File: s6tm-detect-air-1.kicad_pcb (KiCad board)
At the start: 2 copper layers, 0 parts

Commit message: pcb: add missing 3dmodels
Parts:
- added C1: 1u, Capacitor_SMD:C_0402_1005Metric, F.Cu at (73.8, 151.6)
- added C10: 0u1, Capacitor_SMD:C_0402_1005Metric, F.Cu at (76.7, 151.6)
- added C11: 0u1, Capacitor_SMD:C_0402_1005Metric, F.Cu at (76.7, 153.6)
- added C12: 0u1, Capacitor_SMD:C_0402_1005Metric, F.Cu at (76.7, 155.6)
- added C13: 0u1, Capacitor_SMD:C_0402_1005Metric, F.Cu at (76.7, 157.5)
- added C14: 0u1, Capacitor_SMD:C_0402_1005Metric, F.Cu at (79.6, 151.6)
- added C15: 1u, Capacitor_SMD:C_0402_1005Metric, F.Cu at (79.6, 153.6)
- added C16: 1u, Capacitor_SMD:C_0402_1005Metric, F.Cu at (79.6, 155.6)
- added C17: 0u1, Capacitor_SMD:C_0402_1005Metric, F.Cu at (79.6, 157.5)
- added C18: 1u, Capacitor_SMD:C_0402_1005Metric, F.Cu at (82.5, 151.6)
- added C19: 0u1, Capacitor_SMD:C_0402_1005Metric, F.Cu at (82.5, 153.6)
- added C2: 10u, Capacitor_SMD:C_0805_2012Metric, F.Cu at (63.3, 163.5)
- added C20: 1u, Capacitor_SMD:C_0402_1005Metric, F.Cu at (82.5, 155.6)
- added C21: 22u, Capacitor_SMD:C_0805_2012Metric, F.Cu at (63.3, 172.5)
- added C22: 0u1, Capacitor_SMD:C_0402_1005Metric, F.Cu at (82.5, 157.5)
- added C23: 22u, Capacitor_SMD:C_0805_2012Metric, F.Cu at (63.3, 175.5)
- added C24: 22u, Capacitor_SMD:C_0805_2012Metric, F.Cu at (63.3, 178.6)
- added C3: 0u1, Capacitor_SMD:C_0402_1005Metric, F.Cu at (73.8, 153.6)
- added C4: 1u, Capacitor_SMD:C_0402_1005Metric, F.Cu at (73.8, 155.6)
- added C5: 10u, Capacitor_SMD:C_0805_2012Metric, F.Cu at (63.3, 166.5)
- added C6: 0u1, Capacitor_SMD:C_0402_1005Metric, F.Cu at (73.8, 157.5)
- added C7: 10u, Capacitor_SMD:C_0805_2012Metric, F.Cu at (63.3, 169.5)
- added C8: 20p, Capacitor_SMD:C_0603_1608Metric, F.Cu at (69.1, 140.4)
- added C9: 20p, Capacitor_SMD:C_0603_1608Metric, F.Cu at (69.1, 142.9)
- added D1: H5VU10U, GLCS:Diode_DFN1006, F.Cu at (59.4, 165.2)
- added D2: H5VU10U, GLCS:Diode_DFN1006, F.Cu at (59.4, 167.2)
- added D3: H5VU10U, GLCS:Diode_DFN1006, F.Cu at (59.4, 169.2)
- added D4: H5VU10U, GLCS:Diode_DFN1006, F.Cu at (59.4, 171.2)
- added D5: H5VU10U, GLCS:Diode_DFN1006, F.Cu at (59.4, 173.2)
- added D6: H5VU10U, GLCS:Diode_DFN1006, F.Cu at (59.4, 175.1)
- added D7: YELLOW, LED_SMD:LED_0805_2012Metric, F.Cu at (55.0, 178.5)
- added D8: SMAJ12A, Diode_SMD:D_SMA, F.Cu at (75.2, 146.5)
- added D9: GREEN, LED_SMD:LED_0805_2012Metric, F.Cu at (55.0, 181.5)
- added FB1: 600Ω@100M, Inductor_SMD:L_0805_2012Metric, F.Cu at (74.7, 159.9)
- added J1: Conn_01x04, Connector_PinHeader_2.54mm:PinHeader_1x04_P2.54mm_Horizontal, F.Cu at (35.5, 152.9)
- added J2: TC2030, Connector:Tag-Connect_TC2030-IDC-NL_2x03_P1.27mm_Vertical, F.Cu at (75.2, 141.7)
- added J3: Conn_01x04, Connector_PinHeader_2.54mm:PinHeader_1x04_P2.54mm_Horizontal, F.Cu at (35.5, 165.2)
- added J4: Conn_01x04, Connector_JST:JST_XH_S4B-XH-A-1_1x04_P2.50mm_Horizontal, F.Cu at (50.1, 155.6)
- added J5: Conn_01x04_Pin, Connector_PinHeader_2.54mm:PinHeader_1x04_P2.54mm_Vertical, F.Cu at (79.2, 164.3)
- added JP1: Jumper_2_Small_Bridged, Jumper:SolderJumper-2_P1.3mm_Open_RoundedPad1.0x1.5mm, F.Cu at (63.2, 181.8)
- added R1: 100, Resistor_SMD:R_0402_1005Metric, F.Cu at (75.4, 163.0)
- added R10: 5k1, Resistor_SMD:R_0402_1005Metric, F.Cu at (75.4, 171.0)
- added R11: 1k, Resistor_SMD:R_0402_1005Metric, F.Cu at (75.4, 172.9)
- added R12: 2k, Resistor_SMD:R_0402_1005Metric, F.Cu at (75.4, 174.9)
- added R13: 5k1, Resistor_SMD:R_0402_1005Metric, F.Cu at (75.4, 176.9)
- added R2: 33, Resistor_SMD:R_0603_1608Metric, F.Cu at (69.1, 145.4)
- added R3: 1M, Potentiometer_THT:Potentiometer_Bourns_3296W_Vertical, F.Cu at (54.7, 167.4)
- added R4: 1M, Potentiometer_THT:Potentiometer_Bourns_3296W_Vertical, F.Cu at (54.7, 173.8)
- added R5: 10k, Resistor_SMD:R_0402_1005Metric, F.Cu at (75.4, 165.0)
- added R6: 10k, Resistor_SMD:R_0402_1005Metric, F.Cu at (75.4, 167.0)
- added R7: 10k, Resistor_SMD:R_0402_1005Metric, F.Cu at (75.4, 169.0)
- added R8: 560, Resistor_SMD:R_0603_1608Metric, F.Cu at (69.1, 147.9)
- added R9: 120, Resistor_SMD:R_1206_3216Metric, F.Cu at (77.5, 136.4)
- added SW1: SW_Push, Button_Switch_SMD:SW_SPST_TS-1088-xR020, F.Cu at (80.4, 176.5)
- added SW2: SW_Push, Button_Switch_SMD:SW_SPST_TS-1088-xR020, F.Cu at (80.4, 181.0)
- added TP1: TestPoint, TestPoint:TestPoint_Pad_D2.0mm, F.Cu at (35.3, 177.1)
- added TP2: TestPoint, TestPoint:TestPoint_Pad_D2.0mm, F.Cu at (35.3, 181.1)
- added TP3: TestPoint, TestPoint:TestPoint_Pad_D2.0mm, F.Cu at (39.3, 177.1)
- added TP4: TestPoint, TestPoint:TestPoint_Pad_D2.0mm, F.Cu at (39.3, 181.1)
- added TP5: TestPoint, TestPoint:TestPoint_Pad_D2.0mm, F.Cu at (43.4, 177.1)
- added TP6: TestPoint, TestPoint:TestPoint_Pad_D2.0mm, F.Cu at (43.4, 181.1)
- added U1: SYS1002-H2, Crystal:Crystal_SMD_3225-4Pin_3.2x2.5mm, F.Cu at (68.1, 177.4)
- added U10: 004-1-0100, Sensor:Senseair_S8_Up, F.Cu at (35.4, 135.0)
- added U2: MiCS-5524, Sensor:Sensortech_MiCS_5x7mm_P1.25mm, F.Cu at (70.9, 134.3)
- added U3: LMC6482, Package_SO:SOIC-8_3.9x4.9mm_P1.27mm, F.Cu at (69.7, 165.4)
- added U4: HT753-1, Package_TO_SOT_SMD:SOT-89-3, F.Cu at (50.0, 180.1)
- added U5: SN65HVD230, Package_SO:SOIC-8_3.9x4.9mm_P1.27mm, F.Cu at (69.7, 171.9)
- added U6: STM32F103C8Tx, Package_QFP:LQFP-48_7x7mm_P0.5mm, F.Cu at (66.7, 156.3)
- added U7: HTU21, Package_SON:Texas_PWSON-N6, F.Cu at (68.0, 182.1)
- added U8: LM73100, GLCS:Texas_RPW0010A_VQFN-HR-10_2x2mm_P0.5mm, F.Cu at (81.3, 141.2)
- added U9: ENS16x, GLCS:Sciosense_ENS160_LGA_9_3x3mm, F.Cu at (81.5, 146.5)
- added Y1: 8M, Crystal:Crystal_SMD_5032-2Pin_5.0x3.2mm, F.Cu at (78.3, 132.1)

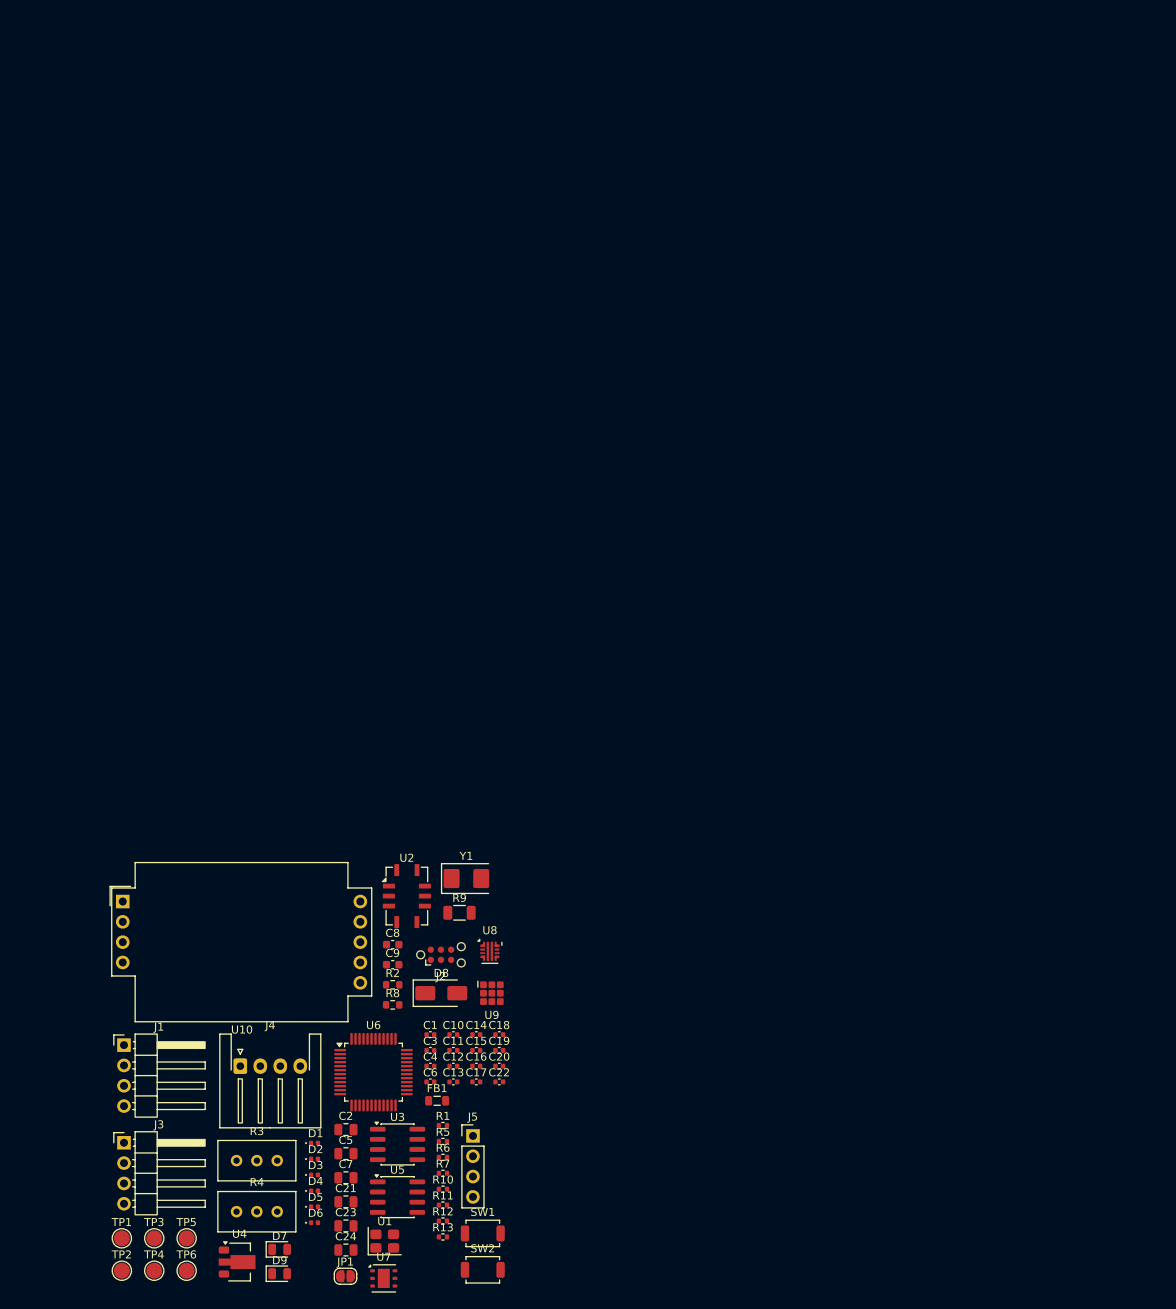
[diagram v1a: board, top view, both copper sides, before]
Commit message: pcb: initial sectionning
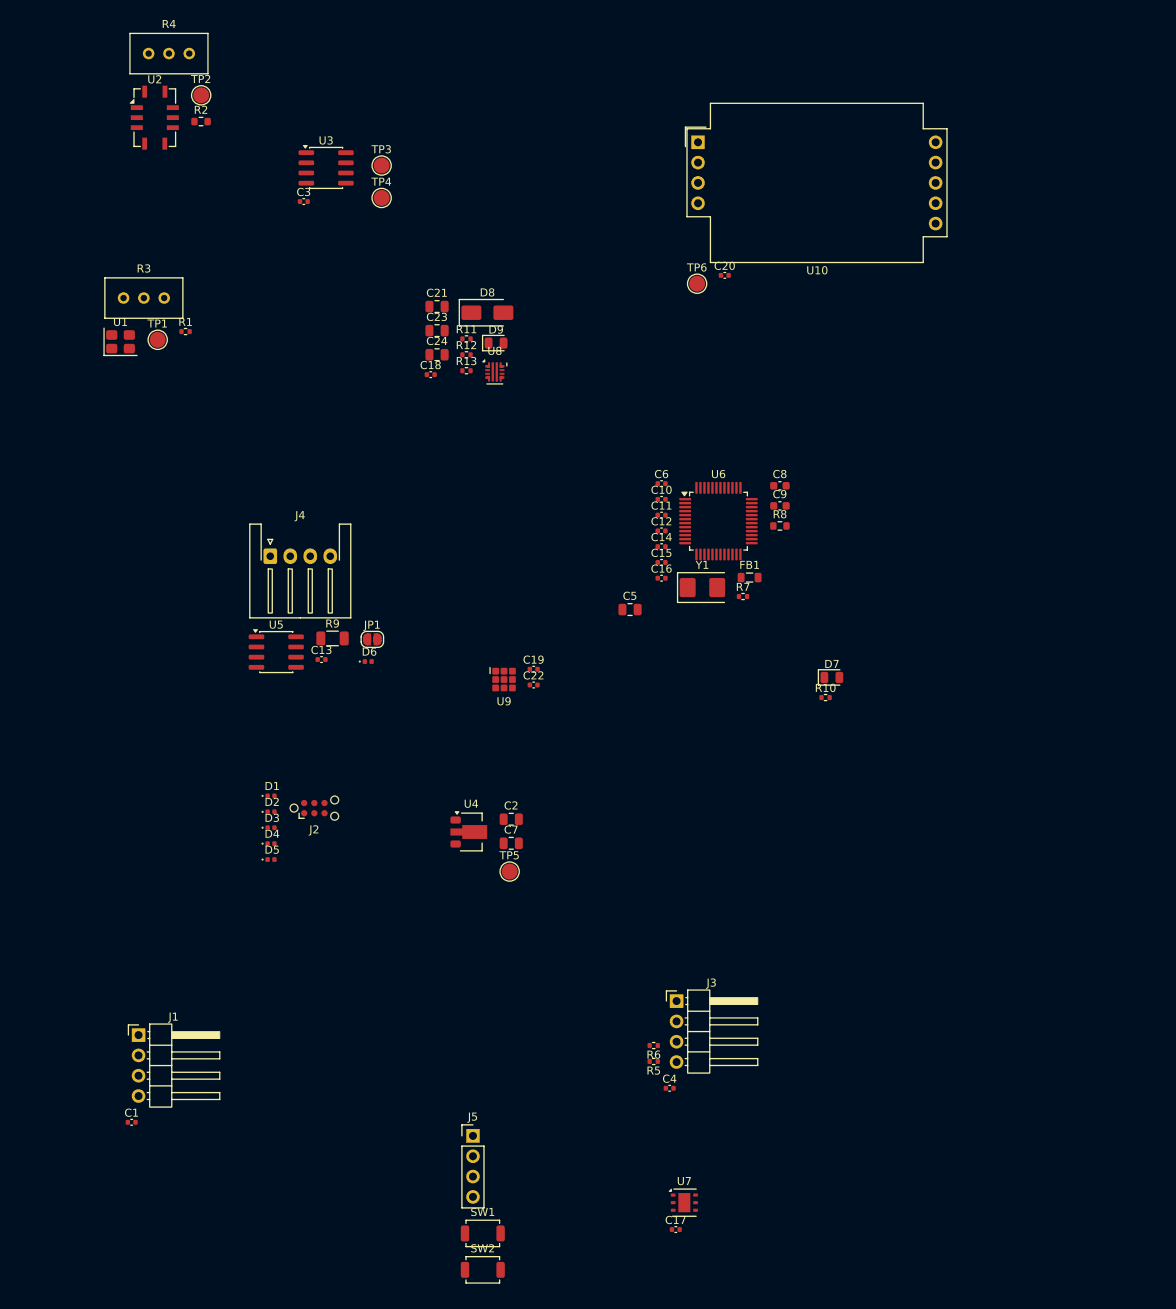
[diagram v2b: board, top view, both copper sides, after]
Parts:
- moved TP2 147.3 mm to (45.2, 34.2)
- moved R4 145.2 mm to (43.7, 29.0)
- moved TP6 138.9 mm to (107.2, 57.8)
- moved TP4 137.1 mm to (67.8, 47.0)
- moved TP3 137.1 mm to (67.8, 43.0)
- moved U3 122.4 mm to (60.8, 43.3)
- moved D9 119.4 mm to (82.1, 65.2)
- moved U10 119.1 mm to (107.3, 40.1)
- moved U1 117.2 mm to (35.1, 65.0)
- moved C24 112.5 mm to (74.7, 66.6)
- moved C21 112.5 mm to (74.7, 60.6)
- moved C23 112.5 mm to (74.7, 63.6)
- moved TP1 112.4 mm to (39.8, 64.8)
- moved R2 110.5 mm to (45.2, 37.5)
- moved R3 108.7 mm to (40.6, 59.6)
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
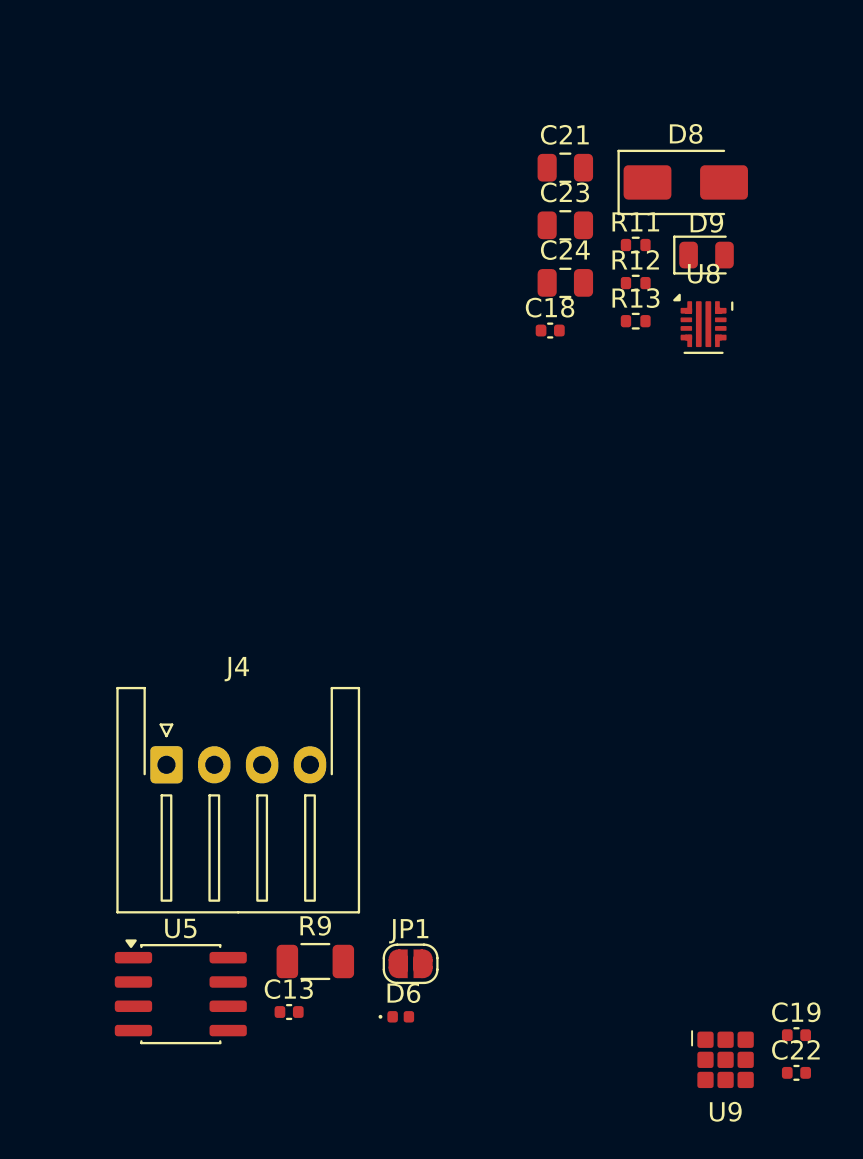
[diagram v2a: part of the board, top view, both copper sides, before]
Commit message: pcb: add can and efuse layout
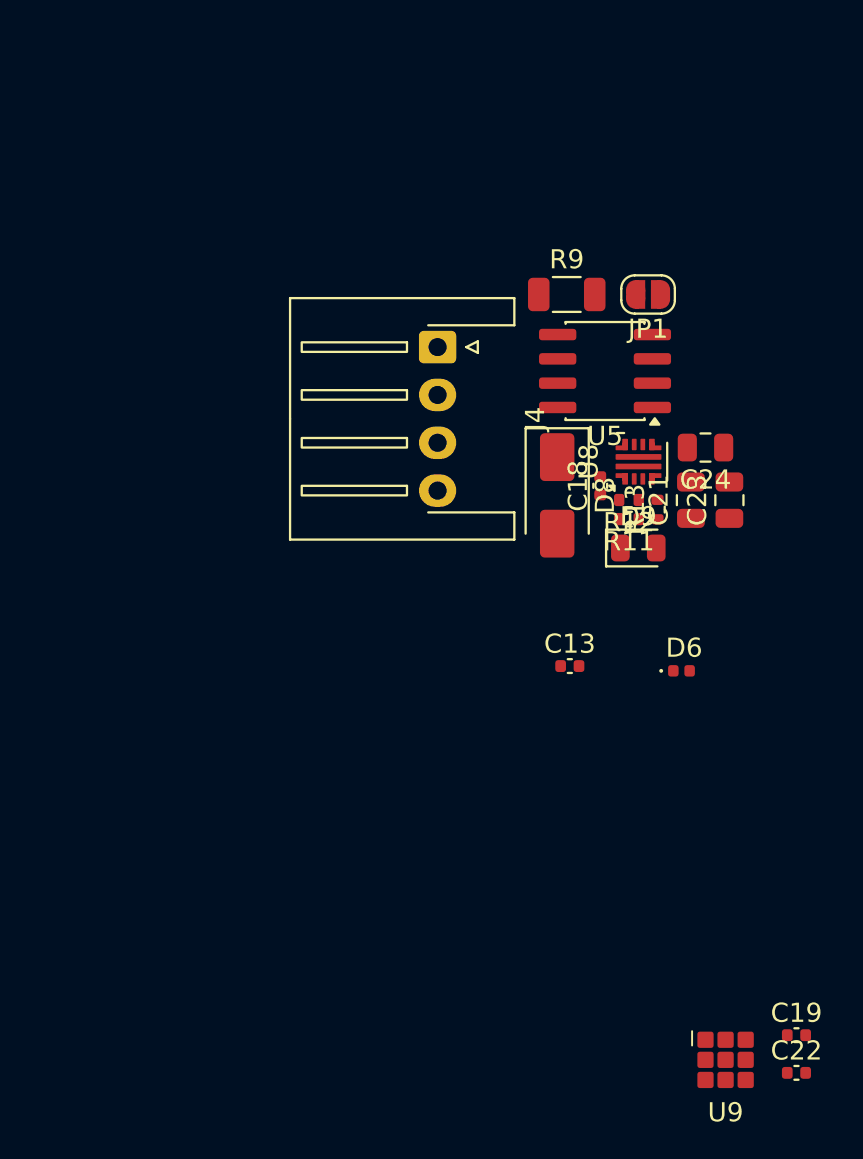
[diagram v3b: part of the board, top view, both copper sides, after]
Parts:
- moved U5 39.4 mm to (76.8, 71.2), turned to 180 degrees
- moved R9 37.3 mm to (74.8, 67.2)
- moved JP1 37.1 mm to (79.0, 67.2), turned to 180 degrees
- moved J4 26.0 mm to (68.0, 70.0), turned to -90 degrees
- moved D6 23.3 mm to (80.7, 86.9)
- moved C13 23.3 mm to (74.9, 86.7)
- moved C21 18.6 mm to (81.2, 78.0), turned to 90 degrees
- moved D8 17.7 mm to (74.2, 77.8), turned to -90 degrees
- moved C23 16.7 mm to (83.2, 78.0), turned to 90 degrees
- moved D9 15.7 mm to (78.5, 80.5)
- moved R11 14.3 mm to (78.0, 79.0), turned to 180 degrees
- moved R12 11.3 mm to (78.0, 78.0), turned to 180 degrees
- moved C24 11.3 mm to (82.0, 75.2), turned to 180 degrees
- moved R13 9.91 mm to (79.5, 78.5), turned to 90 degrees
- moved C18 8.53 mm to (76.5, 77.2), turned to 90 degrees
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
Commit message: pcb: add mox layout
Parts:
- moved R1 30.8 mm to (24.2, 39.5), turned to 90 degrees
- moved U1 26.4 mm to (28.5, 39.5), turned to 180 degrees
- moved TP1 21.7 mm to (29.8, 45.5)
- moved R4 21.5 mm to (40.5, 50.2)
- moved R3 14.1 mm to (30.0, 50.2)
- moved TP2 13.9 mm to (37.0, 45.5)
- moved U2 2.74 mm to (38.2, 39.5), turned to 90 degrees
- moved R2 1.05 mm to (44.2, 38.0), turned to 90 degrees
- moved U3 0.82 mm to (61.0, 42.5)

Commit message: pcb: add pwr layout
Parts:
- removed D6: H5VU10U, GLCS:Diode_DFN1006
- moved C2 51.0 mm to (86.5, 73.8), turned to 180 degrees
- moved U4 49.8 mm to (87.5, 77.2)
- moved C7 47.0 mm to (86.5, 80.8)
- moved C13 16.6 mm to (81.0, 71.3), turned to -90 degrees

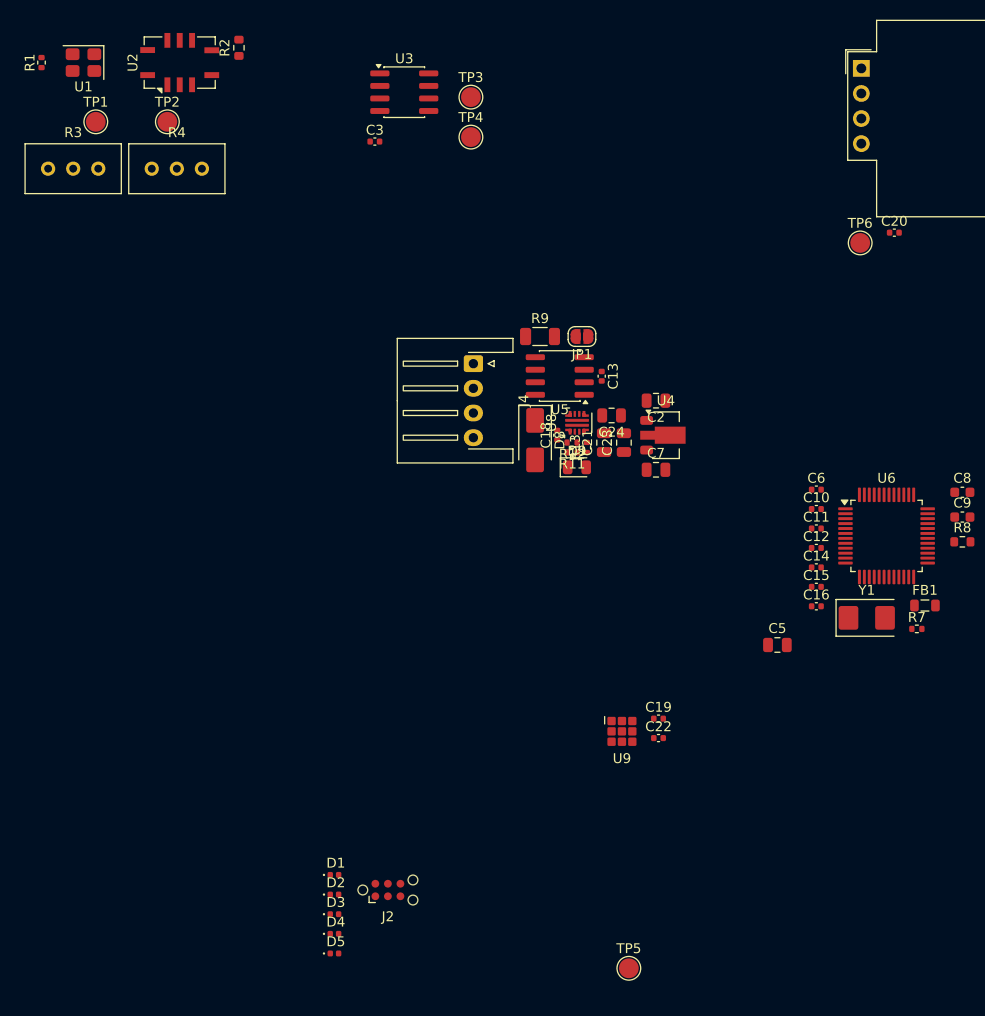
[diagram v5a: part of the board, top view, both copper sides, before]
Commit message: pcb: add ens160 layout
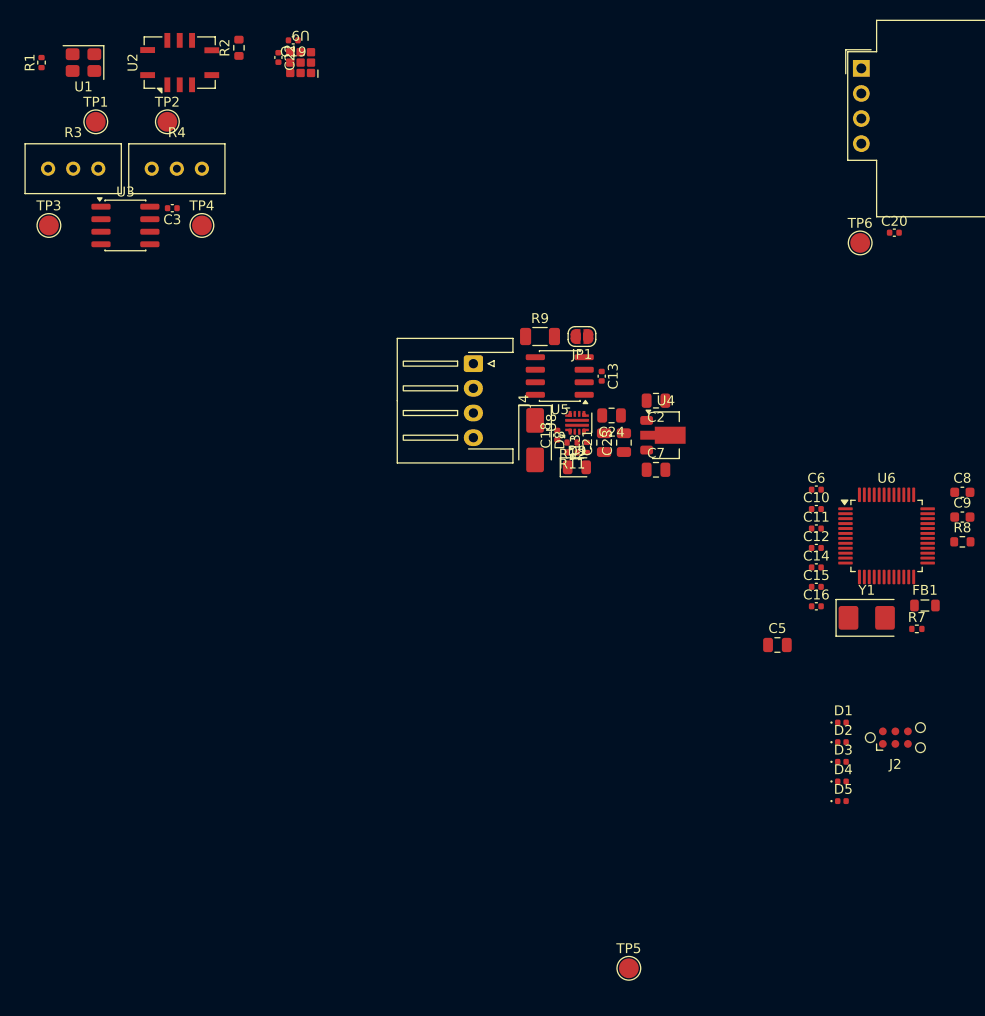
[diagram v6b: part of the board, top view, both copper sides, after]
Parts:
- moved C22 79.0 mm to (48.2, 39.0), turned to -90 degrees
- moved C19 78.0 mm to (49.8, 37.2), turned to 180 degrees
- moved U9 75.2 mm to (50.5, 39.5), turned to 180 degrees
- moved D1 53.7 mm to (105.3, 106.4)
- moved D2 53.7 mm to (105.3, 108.3)
- moved D3 53.7 mm to (105.3, 110.3)
- moved D4 53.7 mm to (105.3, 112.3)
- moved D5 53.7 mm to (105.3, 114.3)
- moved J2 53.7 mm to (110.8, 107.9)
- moved TP3 44.7 mm to (25.0, 56.0)
- moved U3 31.3 mm to (32.8, 56.0)
- moved TP4 28.7 mm to (40.5, 56.0)
- moved C3 21.6 mm to (37.5, 54.2), turned to 180 degrees
